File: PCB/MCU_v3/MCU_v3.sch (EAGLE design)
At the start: 42 parts, among them IC1 ATMEGA2560-16AU, U2 HC_05

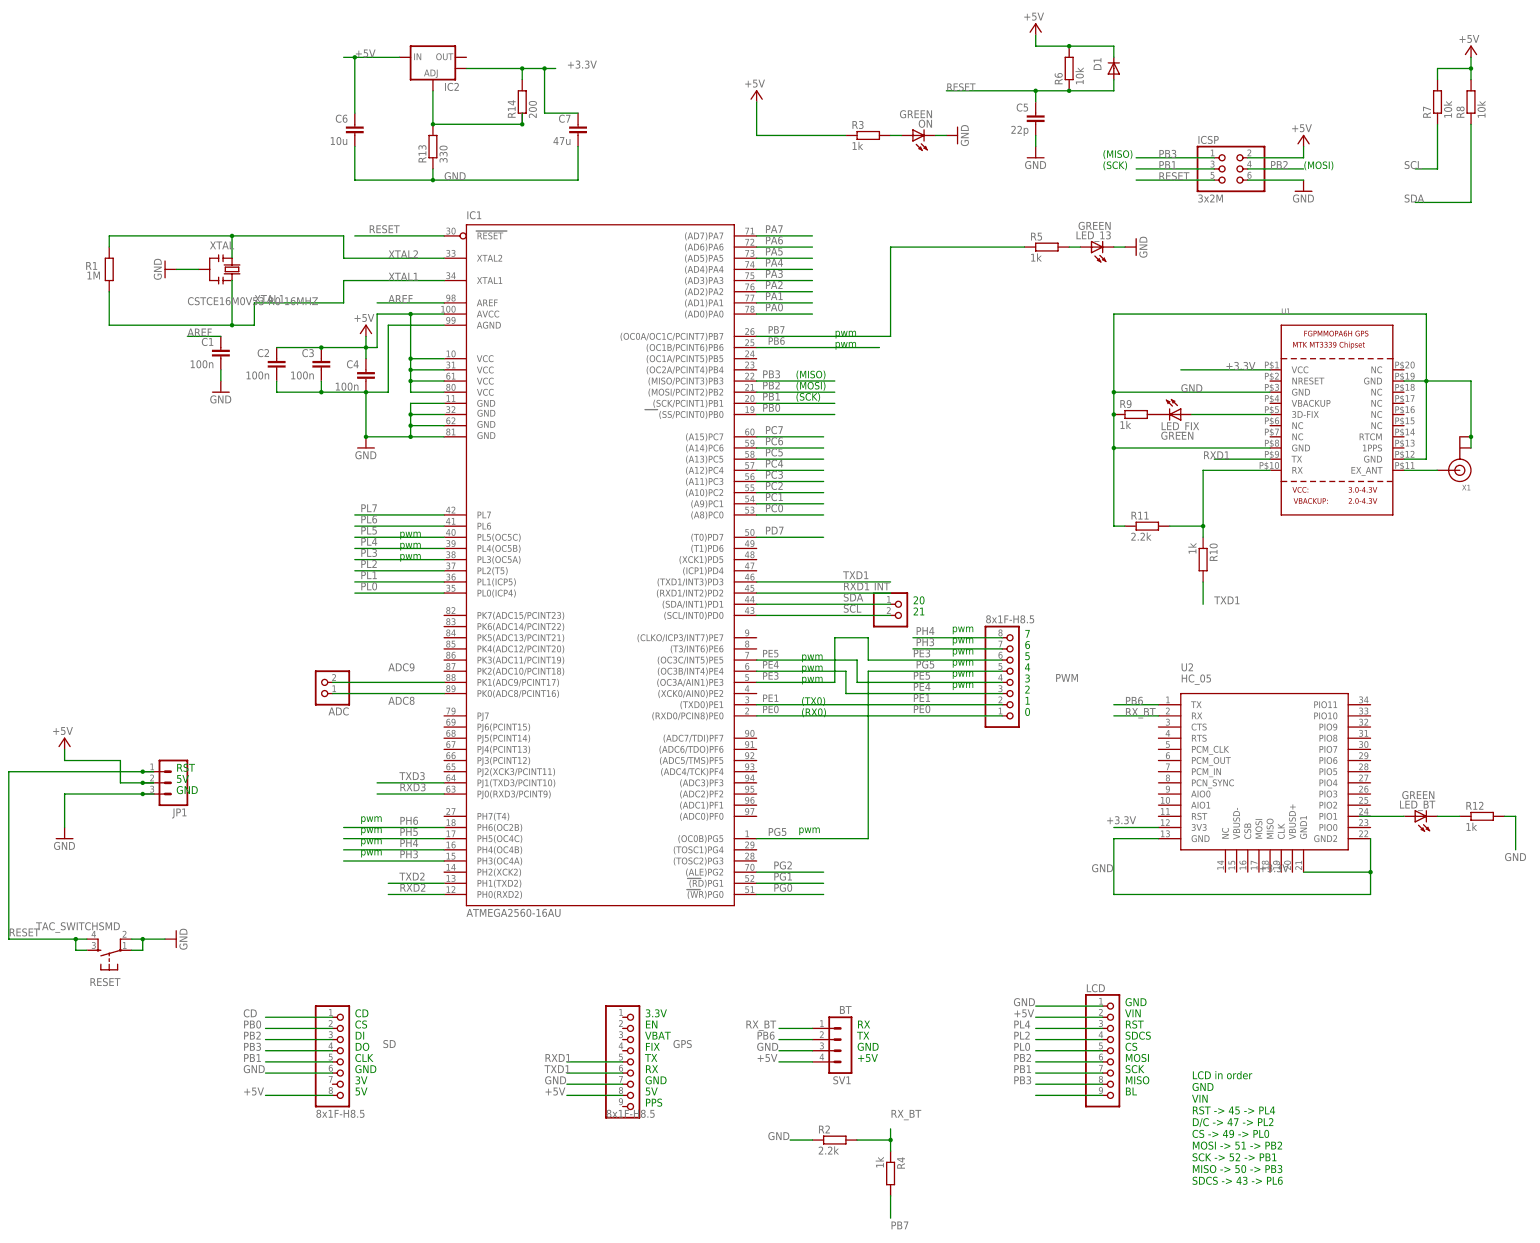
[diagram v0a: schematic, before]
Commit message: RPM updated for all gear combinations
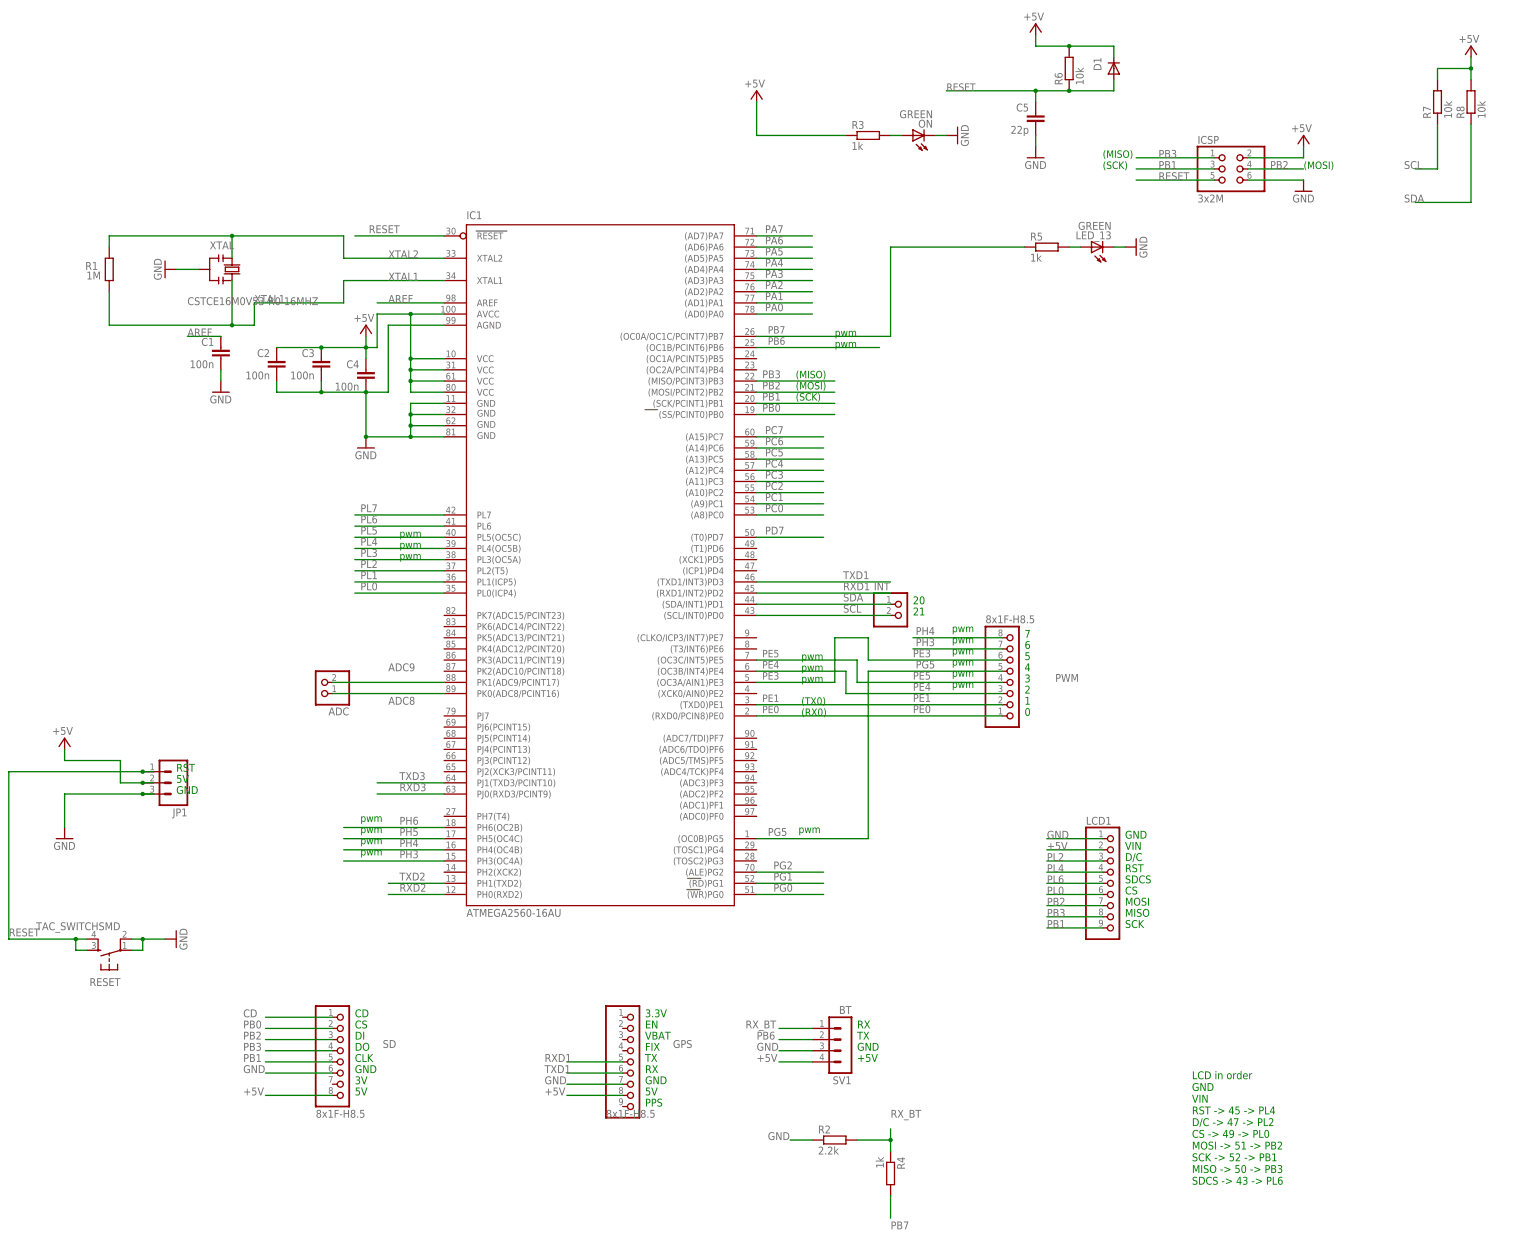
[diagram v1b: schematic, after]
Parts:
- removed C6: 10u, resistor:C-EUC0805
- removed C7: 47u, resistor:C-EUC0805
- removed IC2: (no value), SparkFun-PowerIC:V_REG_LM1117SOT223
- removed LCD: (no value), pinhead:PINHD-1X9
- removed LED_BT, LED_FIX: GREEN, led:LEDCHIP-LED0805
- removed R10, R12, R9: 1k, resistor:R-EU_R0805
- removed R11: 2.2k, resistor:R-EU_R0805
- removed R13: 330, resistor:R-EU_R0805
- removed R14: 200, resistor:R-EU_R0805
- removed U1: (no value), adafruit:GPS_FGPMMOPA6H
- removed U2: HC_05, SerialPortBluetooth:HC_05
- removed X1: (no value), adafruit:ANTENNA_U.FL
- added LCD1: (no value), pinhead:PINHD-1X9
- JP1: MPN (none) -> BI2-Q10S-AZ31X-0.3M-SB3T; OC_NEWARK (none) -> 31Y7711
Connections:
- removed net +3.3V: C7.1, IC2.OUT@1, R14.2, U1.VCC, U2.3V3
- removed net N$15: LCD.9
- removed net N$2: LED_FIX.A, U1.3D-FIX
- removed net N$4: LED_FIX.C, R9.2
- removed net N$5: R10.1, R11.2, U1.RX
- removed net N$6: U1.EX_ANT, X1.SIGNAL
- removed net N$7: LED_BT.A
- removed net N$8: LED_BT.C, R12.1
- removed net N$9: IC2.ADJ, R13.2, R14.1
- net +5V: now also LCD1.2; no longer C6.1, IC2.IN, LCD.2
- net GND: now also LCD1.1; no longer C6.2, C7.2, LCD.1, R11.1, R12.2, R13.1, R9.1, U1.GND@1, U1.GND@2, U1.GND@3, U1.GND@4, U2.GND, U2.GND1, U2.GND2, X1.GND@0, X1.GND@1
- net PB1: now also LCD1.9; no longer LCD.7
- net PB2: now also LCD1.7; no longer LCD.6
- net PB3: now also LCD1.8; no longer LCD.8
- net PB6: no longer U2.TX
- net PL0: now also LCD1.6; no longer LCD.5
- net PL2: now also LCD1.3; no longer LCD.4
- net PL4: now also LCD1.4; no longer LCD.3
- net PL6: now also LCD1.5
- net RXD1: no longer U1.TX
- net RX_BT: no longer U2.RX
- net TXD1: no longer R10.2
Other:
- note added: "D/C"
- note removed: "BL"
